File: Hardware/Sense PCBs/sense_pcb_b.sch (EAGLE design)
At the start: 32 parts, among them J1 DF11-18DP-2DSA(24)

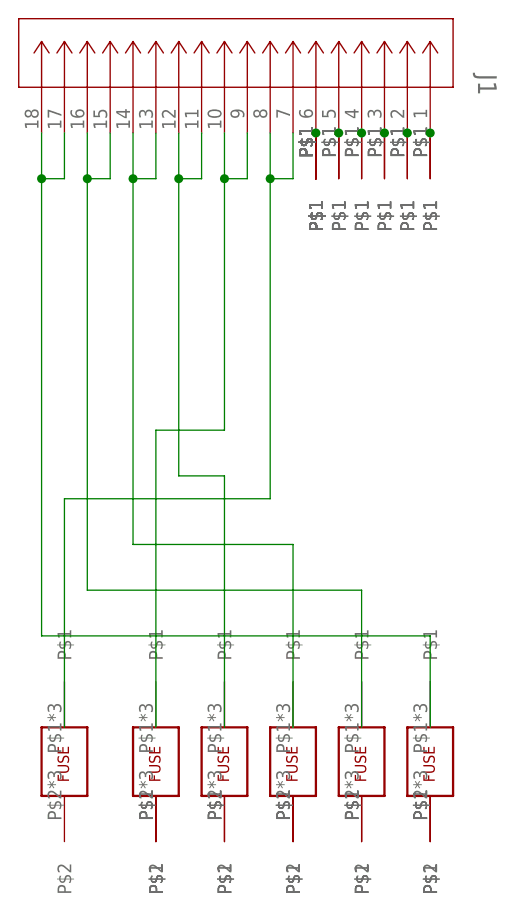
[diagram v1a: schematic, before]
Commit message: fixed outline, updated gerbers
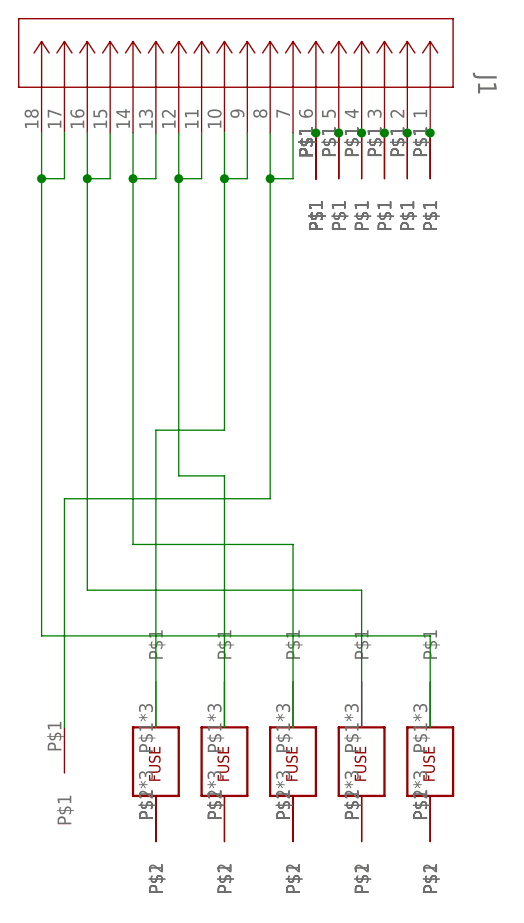
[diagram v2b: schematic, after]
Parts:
- U$11: value FUSE -> BB_CONTACT; device sense_pcb_components:FUSE -> sense_pcb_components:BB_CONTACT
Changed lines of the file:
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@@
 <part name="U$9" library="sense_pcb_components" deviceset="BB_CONTACT" device=""/>
 <part name="U$10" library="sense_pcb_components" deviceset="BB_CONTACT" device=""/>
-<part name="U$11" library="sense_pcb_components" deviceset="FUSE" device=""/>
 <part name="U$12" library="sense_pcb_components" deviceset="THERM_PIN" device=""/>
 <part name="U$13" library="sense_pcb_components" deviceset="THERM_PIN" device=""/>
@@
 <part name="U$30" library="sense_pcb_components" deviceset="THERM_PIN" device=""/>
 <part name="U$31" library="sense_pcb_components" deviceset="THERM_PIN" device=""/>
+<part name="U$11" library="sense_pcb_components" deviceset="BB_CONTACT" device=""/>
 </parts>
 <sheets>
@@
 <instance part="U$9" gate="G$1" x="27.94" y="10.16" smashed="yes" rot="R270"/>
 <instance part="U$10" gate="G$1" x="35.56" y="10.16" smashed="yes" rot="R270"/>
-<instance part="U$11" gate="G$1" x="-5.08" y="7.62" smashed="yes" rot="R90"/>
 <instance part="U$12" gate="G$1" x="22.86" y="83.82" smashed="yes" rot="R270"/>
 <instance part="U$13" gate="G$1" x="22.86" y="83.82" smashed="yes" rot="R270"/>
@@
 <instance part="U$30" gate="G$1" x="35.56" y="83.82" smashed="yes" rot="R270"/>
 <instance part="U$31" gate="G$1" x="35.56" y="83.82" smashed="yes" rot="R270"/>
+<instance part="U$11" gate="G$1" x="-5.08" y="17.78" smashed="yes" rot="R270"/>
 </instances>
 <busses>
@@
 <net name="N$1" class="0">
 <segment>
-<pinref part="U$11" gate="G$1" pin="P$1"/>
 <wire x1="-5.08" y1="17.78" x2="-5.08" y2="43.18" width="0.1524" layer="91"/>
 <wire x1="-5.08" y1="43.18" x2="17.78" y2="43.18" width="0.1524" layer="91"/>
@@
 <pinref part="J1" gate="A" pin="7"/>
 <wire x1="20.32" y1="78.74" x2="20.32" y2="83.82" width="0.1524" layer="91"/>
+<pinref part="U$11" gate="G$1" pin="P$1"/>
 </segment>
 </net>
